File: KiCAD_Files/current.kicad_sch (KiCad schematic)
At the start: 10 parts, among them U3 ACS724xLCTR-10AB, U304 MCP6486UT-E/LT

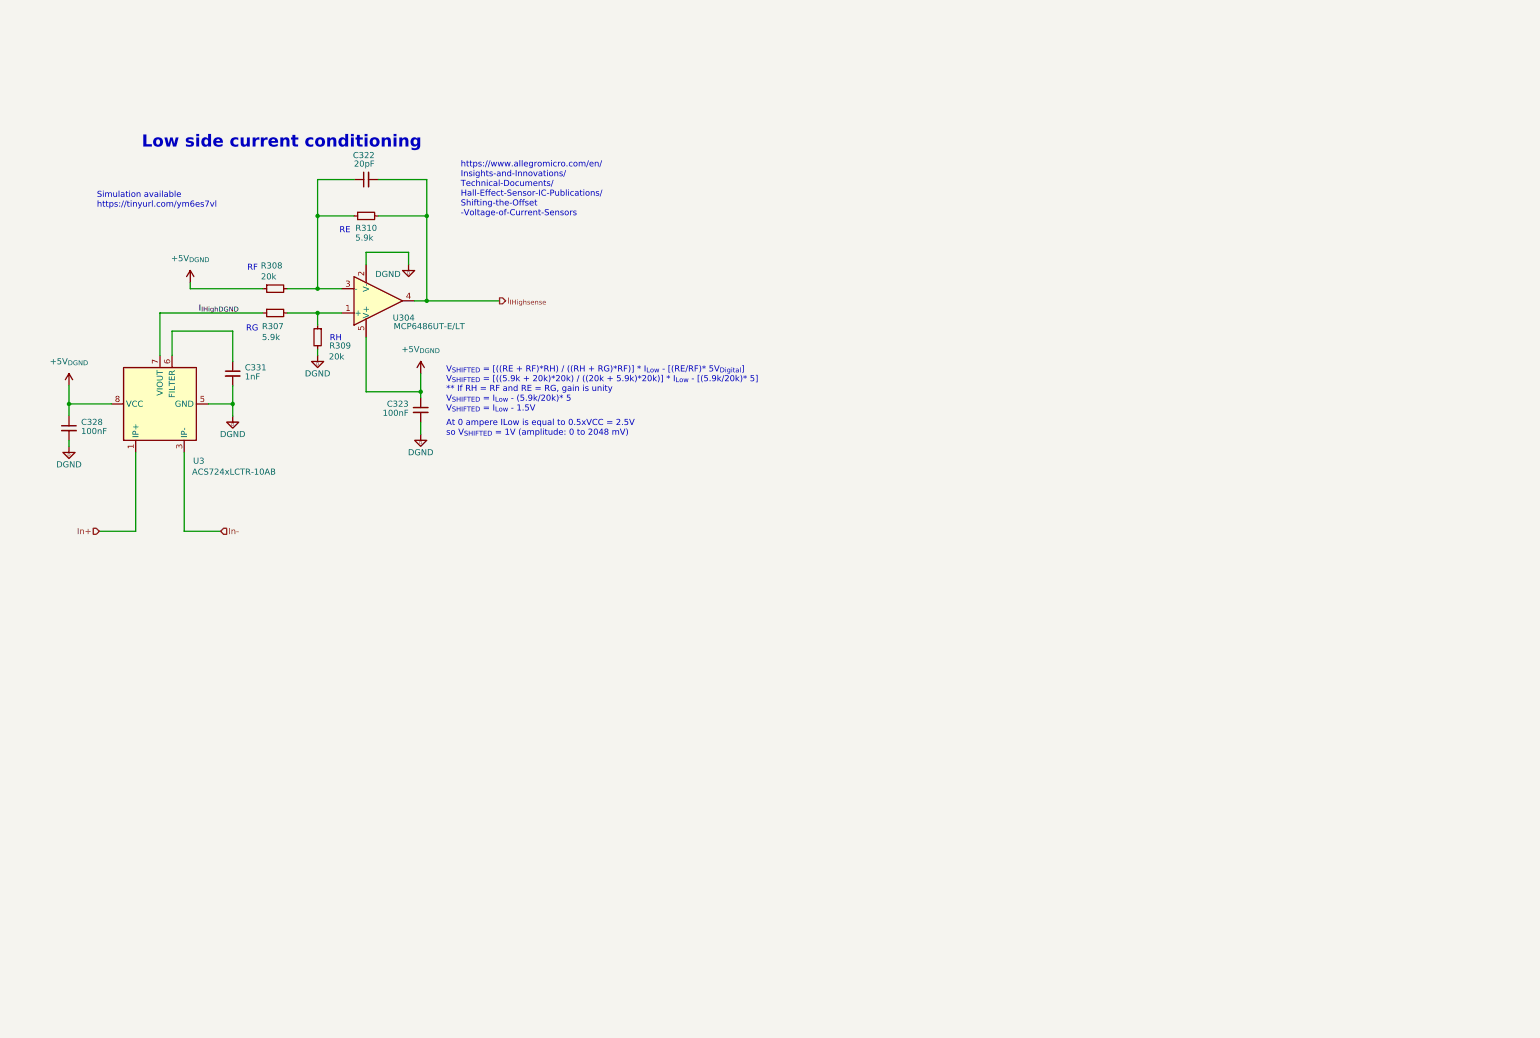
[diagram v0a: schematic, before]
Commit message: Schematic close to completion.
Signed-off-by: Jean Alinei <jean.alinei@owntech.org>
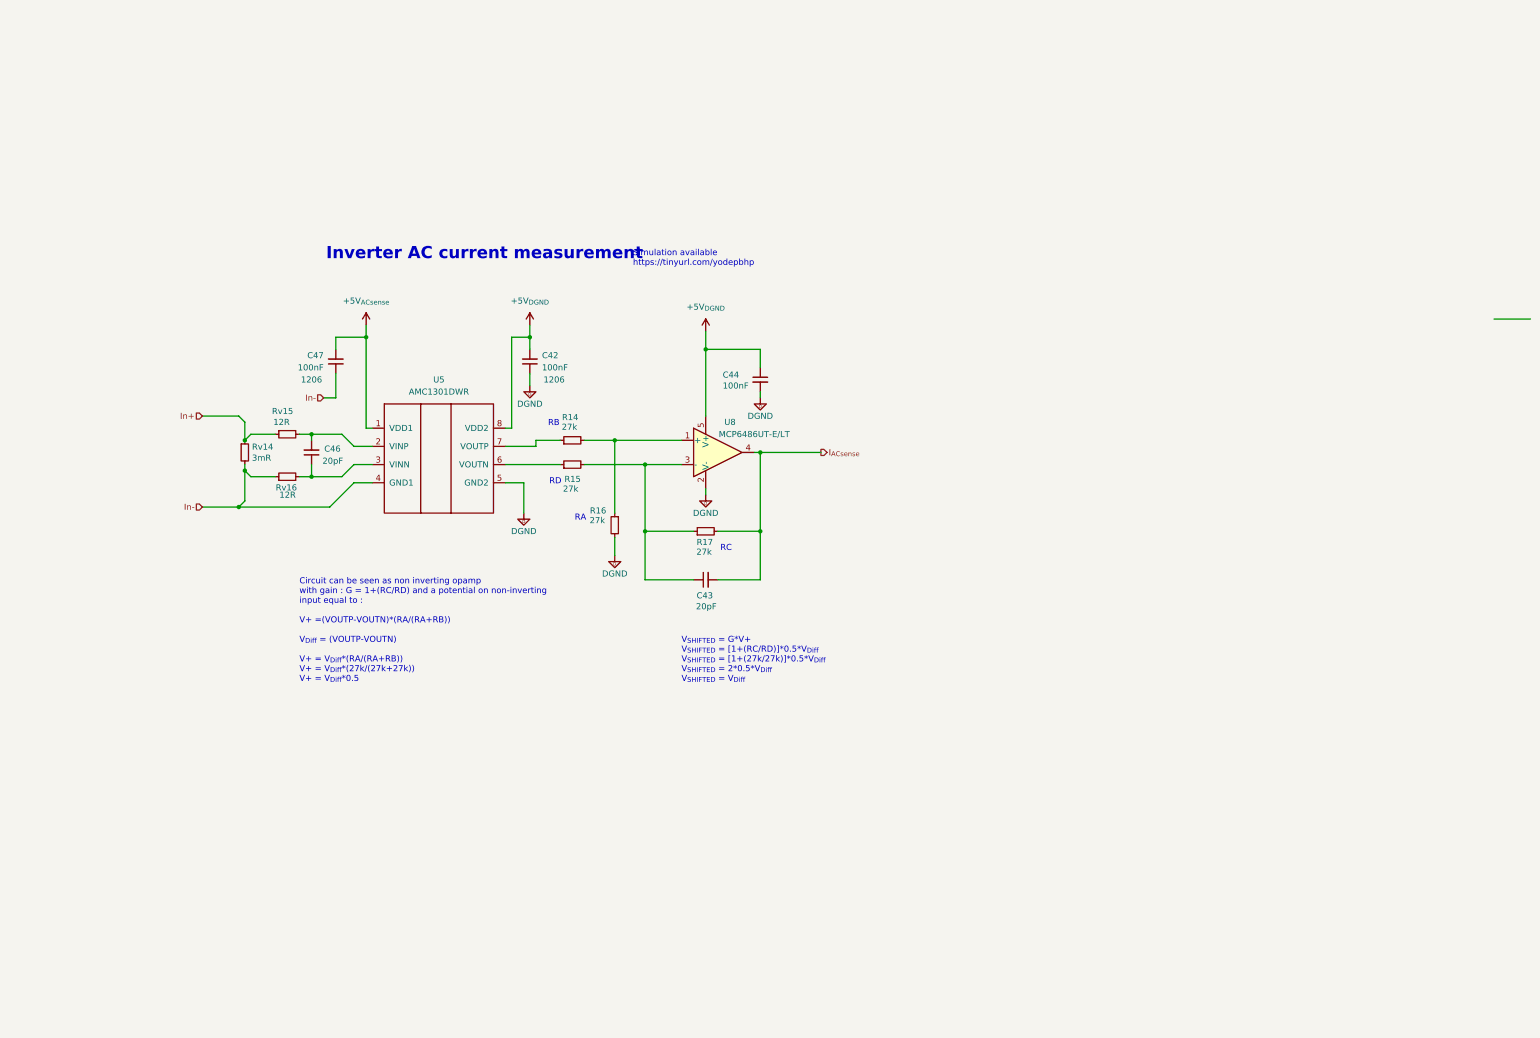
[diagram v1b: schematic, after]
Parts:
- removed C322: 20pF, Footprints:C_0805_2012Metric, symbol Device:C_Small
- removed C323, C328: 100nF, Capacitor_SMD:C_1206_3216Metric, symbol Device:C_Small
- removed C331: 1nF, Capacitor_SMD:C_1206_3216Metric, symbol Device:C_Small
- removed R307, R310: 5.9k, Footprints:R_0805_2012Metric, symbol Device:R_Small
- removed R308, R309: 20k, Footprints:R_0805_2012Metric, symbol Device:R_Small
- removed U3: ACS724xLCTR-10AB, Package_SO:SOIC-8_3.9x4.9mm_P1.27mm, symbol Sensor_Current:ACS724xLCTR-10AB
- removed U304: MCP6486UT-E/LT, Package_TO_SOT_SMD:SOT-353_SC-70-5_Handsoldering, symbol Symbols:MCP6486UT-E/LT
- added C42, C47: 100nF, Capacitor_SMD:C_1206_3216Metric, symbol Device:C_Small
- added C43, C46: 20pF, Footprints:C_0805_2012Metric, symbol Device:C_Small
- added C44: 100nF, Capacitor_SMD:C_0805_2012Metric, symbol Device:C_Small
- added R14, R15, R16, R17: 27k, Footprints:R_0805_2012Metric, symbol Device:R_Small
- added Rv14: 3mR, Resistor_SMD:R_0805_2012Metric, symbol Device:R_Small
- added Rv15, Rv16: 12R, Resistor_SMD:R_0805_2012Metric, symbol Device:R_Small
- added U5: AMC1301DWR, Package_SO:SOIC-8_7.5x5.85mm_P1.27mm, symbol Symbols:AMC1100
- added U8: MCP6486UT-E/LT, Package_TO_SOT_SMD:SOT-353_SC-70-5_Handsoldering, symbol Symbols:MCP6486UT-E/LT
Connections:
- net +5V_{DGND}: now also C42.2, C44.1, U5.8 (VDD2), U8.5 (V+)
- net DGND: now also C42.1, C44.2, R16.2, U5.5 (GND2), U8.2 (V-)
- net In+: now also Rv14.1, Rv15.1
- net In-: now also C47.1, Rv14.2, Rv16.1, U5.4 (GND1)
- new net: R14.1, U5.7 (VOUTP)
- new net: R14.2, R16.1, U8.1 (+)
- new net: C46.2, Rv15.2, U5.2 (VINP)
- new net: R15.1, U5.6 (VOUTN)
- new net: C43.1, R15.2, R17.1, U8.3 (-)
- new net: C46.1, Rv16.2, U5.3 (VINN)
- new net +5V_{ACsense}: C47.2, U5.1 (VDD1)
- new net I_{ACsense}: C43.2, R17.2, U8.4
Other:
- note added: "Circuit can be seen as non inverting opamp with gain : G = 1+(RC/RD) and a potential on non-inverting input equal to : V+ =(VOUTP-VOUTN)*(RA/(RA+RB)) V_{Diff} = (VOUTP-VOUTN) V+ = V_{Diff}*(RA/(RA+RB)) V+ = V_{Diff}*(27k/(27k+27k)) V+ = V_{Diff}*0.5"
- note added: "Inverter AC current measurement"
- note added: "RA"
- note added: "RB"
- note added: "RC"
- note added: "RD"
- note added: "Simulation available https://tinyurl.com/yodepbhp"
- note added: "V_{SHIFTED} = G*V+ V_{SHIFTED} = [1+(RC/RD)]*0.5*V_{Diff} V_{SHIFTED} = [1+(27k/27k)]*0.5*V_{Diff} V_{SHIFTED} = 2*0.5*V_{Diff} V_{SHIFTED} = V_{Diff}"
- note removed: "At 0 ampere ILow is equal to 0.5xVCC = 2.5V so V_{SHIFTED} = 1V (amplitude: 0 to 2048 mV)"
- note removed: "Low side current conditioning"
- note removed: "RE"
- note removed: "RF"
- note removed: "RG"
- note removed: "RH"
- note removed: "Simulation available https://tinyurl.com/ym6es7vl"
- note removed: "V_{SHIFTED} = [((RE + RF)*RH) / ((RH + RG)*RF)] * I_{Low} - [(RE/RF)* 5V_{Digital}] V_{SHIFTED} = [((5.9k + 20k)*20k) / ((20k + 5.9k)*20k)] * I_{Low} - [(5.9k/20k)* 5] ** If RH = RF and RE = RG, gain is unity V_{SHIFTED} = I_{Low} - (5.9k/20k)* 5 V_{SHIFTED} = I_{Low} - 1.5V"
- note removed: "https://www.allegromicro.com/en/ Insights-and-Innovations/ Technical-Documents/ Hall-Effect-Sensor-IC-Publications/ Shifting-the-Offset -Voltage-of-Current-Sensors"

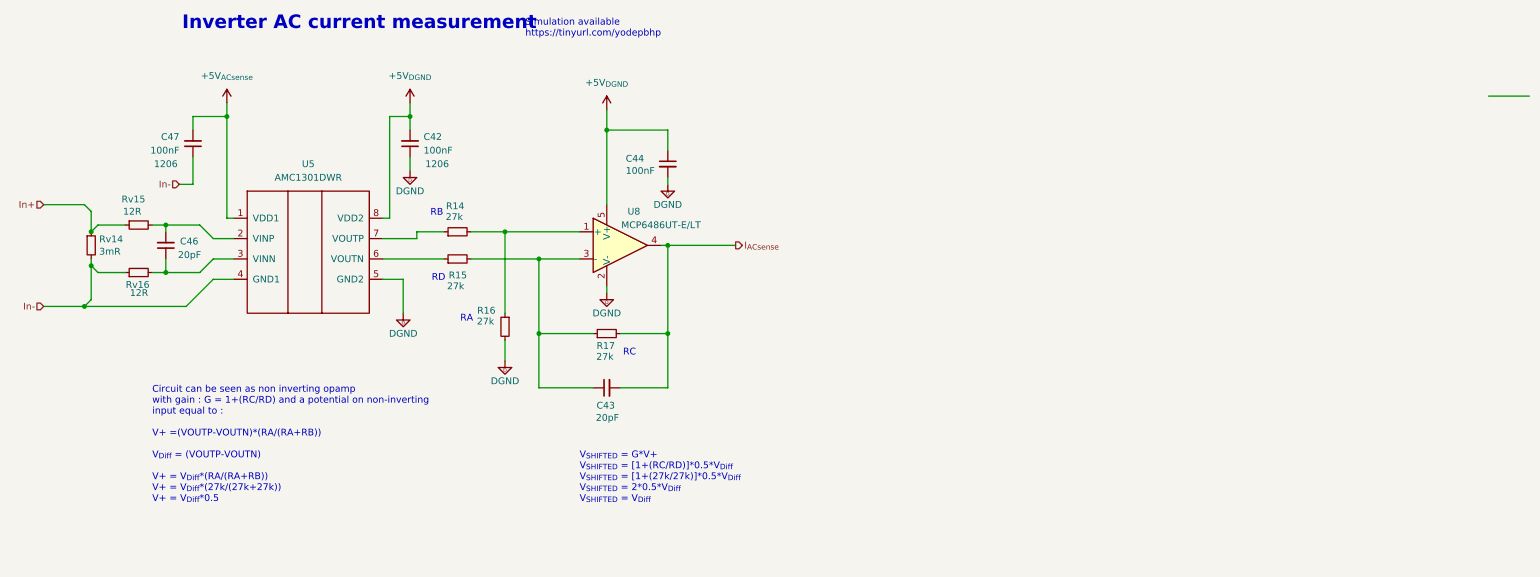
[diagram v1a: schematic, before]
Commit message: First routing pass complete.
Signed-off-by: Jean Alinei <jean.alinei@owntech.org>
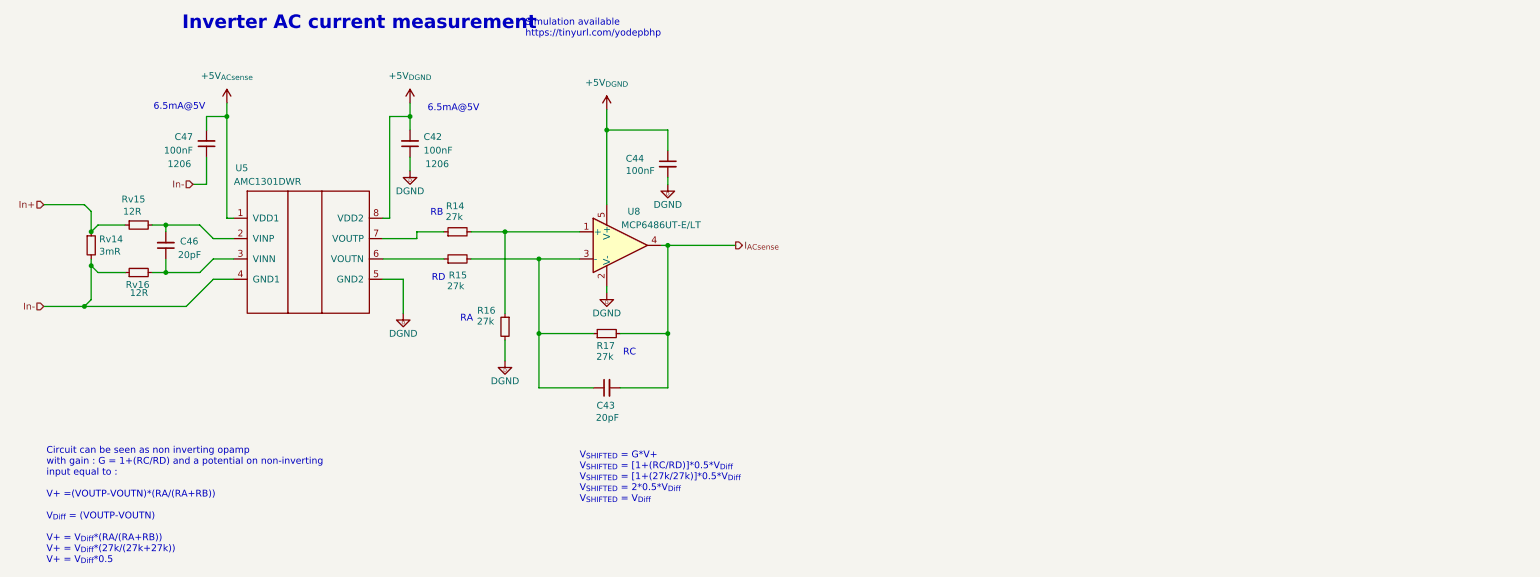
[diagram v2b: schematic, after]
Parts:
- Rv14: footprint Resistor_SMD:R_0805_2012Metric -> Resistor_SMD:R_2512_6332Metric
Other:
- note added: "6.5mA@5V"
- moved on the sheet: C47
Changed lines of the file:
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@@
+		)
+	)
+	(text "6.5mA@5V"
+		(exclude_from_sim no)
+		(at 132.588 84.836 0)
+		(effects
+			(font
+				(size 1.27 1.27)
+				(color 194 0 0 1)
+			)
 		)
 	)
@@
 	(text "Circuit can be seen as non inverting opamp\nwith gain : G = 1+(RC/RD) and a potential on non-inverting\ninput equal to :\n\nV+ =(VOUTP-VOUTN)*(RA/(RA+RB))\n\nV_{Diff} = (VOUTP-VOUTN)\n\nV+ = V_{Diff}*(RA/(RA+RB))\nV+ = V_{Diff}*(27k/(27k+27k))\nV+ = V_{Diff}*0.5"
 		(exclude_from_sim no)
-		(at 76.2 158.75 0)
+		(at 56.388 170.18 0)
 		(effects
 			(font
@@
 			)
 			(justify left bottom)
+		)
+	)
+	(text "6.5mA@5V"
+		(exclude_from_sim no)
+		(at 81.28 84.582 0)
+		(effects
+			(font
+				(size 1.27 1.27)
+				(color 194 0 0 1)
+			)
 		)
 	)
@@
 	(wire
 		(pts
-			(xy 83.82 86.36) (xy 90.17 86.36)
-		)
-		(stroke
-			(width 0)
-			(type default)
-		)
-	)
-	(wire
-		(pts
-			(xy 83.82 99.06) (xy 81.28 99.06)
+			(xy 86.36 86.36) (xy 90.17 86.36)
+		)
+		(stroke
+			(width 0)
+			(type default)
+		)
+	)
+	(wire
+		(pts
+			(xy 86.36 99.06) (xy 83.82 99.06)
 		)
 		(stroke
@@
 	(wire
 		(pts
-			(xy 83.82 93.98) (xy 83.82 99.06)
+			(xy 86.36 93.98) (xy 86.36 99.06)
 		)
 		(stroke
@@
 	(wire
 		(pts
-			(xy 83.82 86.36) (xy 83.82 88.9)
+			(xy 86.36 86.36) (xy 86.36 88.9)
 		)
 		(stroke
@@
 			(width 0)
 			(type default)
-		)
-	)
-	(wire
-		(pts
-			(xy 326.39 82.55) (xy 334.01 82.55)
-		)
-		(stroke
-			(width 0.5)
-			(type default)
-			(color 0 0 255 1)
 		)
 	)
 	(hierarchical_label "In-"
 		(shape input)
-		(at 81.28 99.06 180)
+		(at 83.82 99.06 180)
 		(effects
 			(font
@@
 		)
 	)
+	(rule_area
+		(polyline
+			(pts
+				(xy 105.41 73.66) (xy 105.41 146.05) (xy 200.66 146.05) (xy 200.66 73.66)
+			)
+			(stroke
+				(width 0)
+				(type dash)
+			)
+			(fill
+				(type none)
+			)
+		)
+	)
+	(netclass_flag ""
+		(length 2.54)
+		(shape round)
+		(at 115.57 146.05 0)
+		(fields_autoplaced yes)
+		(effects
+			(font
+				(size 1.27 1.27)
+			)
+			(justify left bottom)
+		)
+		(property "Netclass" "DGND"
+			(at 116.2685 143.51 0)
+			(effects
+				(font
+					(size 1.27 1.27)
+				)
+				(justify left)
+			)
+		)
+		(property "Component Class" ""
+			(at -143.51 97.79 0)
+			(effects
+				(font
+					(size 1.27 1.27)
+					(italic yes)
+				)
+				(hide yes)
+			)
+		)
+	)
 	(symbol
 		(lib_name "R_Small_14")
@@
 		(on_board yes)
 		(dnp no)
-		(fields_autoplaced yes)
 		(property "Reference" "U5"
-			(at 105.41 95.25 0)
+			(at 92.964 96.012 0)
 			(effects
 				(font
@@
 		)
 		(property "Value" "AMC1301DWR"
-			(at 105.41 97.79 0)
+			(at 97.79 98.552 0)
 			(effects
 				(font
@@
 			)
 		)
-		(property "Datasheet" "https://www.ti.com/lit/ds/symlink/amc1100.pdf?ts=1597048467257&ref_url=https%253A%252F%252Fwww.google.com%252F"
+		(property "Datasheet" "${KIPRJMOD}\\datasheets\\amc1301.pdf"
 			(at 105.41 119.38 0)
 			(effects
@@
 	(symbol
 		(lib_id "Device:C_Small")
-		(at 83.82 91.44 180)
+		(at 86.36 91.44 180)
 		(unit 1)
 		(exclude_from_sim no)
@@
 		(dnp no)
 		(property "Reference" "C47"
-			(at 81.28 90.17 0)
+			(at 83.82 90.17 0)
 			(effects
 				(font
@@
 		)
 		(property "Value" "100nF"
-			(at 81.28 92.71 0)
+			(at 83.82 92.71 0)
 			(effects
 				(font
@@
 		)
 		(property "Footprint" "Capacitor_SMD:C_1206_3216Metric"
-			(at 83.82 91.44 0)
+			(at 86.36 91.44 0)
 			(effects
 				(font
@@
 		)
 		(property "Datasheet" "${KIPRJMOD}\\datasheet\\KEM_C1002_X7R_SMD-3316098.pdf"
-			(at 83.82 91.44 0)
+			(at 86.36 91.44 0)
 			(effects
 				(font
@@
 		)
 		(property "Description" ""
-			(at 83.82 91.44 0)
+			(at 86.36 91.44 0)
 			(effects
 				(font
@@
 		)
 		(property "manf#" "C1206C104K5RAC7867"
-			(at 83.82 91.44 0)
+			(at 86.36 91.44 0)
 			(effects
 				(font
@@
 		)
 		(property "DNP" ""
-			(at 83.82 91.44 0)
+			(at 86.36 91.44 0)
 			(effects
 				(font
@@
 		)
 		(property "Voltage" "50V"
-			(at 85.09 87.63 90)
+			(at 87.63 87.63 90)
 			(effects
 				(font
@@
 		)
 		(property "Package" "1206"
-			(at 78.74 95.25 0)
+			(at 81.28 95.25 0)
 			(effects
 				(font
@@
 		)
 		(property "Functional Block" "Measurement"
-			(at 83.82 91.44 0)
+			(at 86.36 91.44 0)
 			(effects
 				(font
@@
 		)
 		(property "Metal content" "BaTiO3"
-			(at 83.82 91.44 0)
+			(at 86.36 91.44 0)
 			(effects
 				(font
@@
 		)
 		(property "Subfunction" "VIHigh measure"
-			(at 83.82 91.44 0)
+			(at 86.36 91.44 0)
 			(effects
 				(font
@@
 		)
 		(property "Dielectric" "X7R"
-			(at 83.82 91.44 0)
+			(at 86.36 91.44 0)
 			(effects
 				(font
@@
 		)
 		(property "Technology" ""
-			(at 83.82 91.44 0)
+			(at 86.36 91.44 0)
 			(effects
 				(font
@@
 		)
 		(property "LCSC" "C5449000"
-			(at 83.82 91.44 0)
+			(at 86.36 91.44 0)
 			(effects
 				(font
@@
 			)
 		)
-		(property "Footprint" "Resistor_SMD:R_0805_2012Metric"
+		(property "Footprint" "Resistor_SMD:R_2512_6332Metric"
 			(at 64.77 110.49 0)
 			(effects

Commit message: Added missing tracks for sensors and relay. Fixed many routing issues.
Signed-off-by: Jean Alinei <jean.alinei@owntech.org>
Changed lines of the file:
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@@
 	(wire
 		(pts
-			(xy 123.19 116.84) (xy 123.19 123.19)
+			(xy 124.46 116.84) (xy 124.46 132.08)
 		)
 		(stroke
@@
 	(wire
 		(pts
-			(xy 119.38 116.84) (xy 123.19 116.84)
+			(xy 119.38 116.84) (xy 124.46 116.84)
 		)
 		(stroke
@@
 	(symbol
 		(lib_id "Symbols:DGND")
-		(at 123.19 123.19 0)
+		(at 124.46 132.08 0)
 		(unit 1)
 		(exclude_from_sim no)
@@
 		(dnp no)
 		(property "Reference" "#PWR026"
-			(at 123.19 129.54 0)
+			(at 124.46 138.43 0)
 			(effects
 				(font
@@
 		)
 		(property "Value" "DGND"
-			(at 123.19 127 0)
+			(at 124.46 135.89 0)
 			(effects
 				(font
@@
 		)
 		(property "Footprint" ""
-			(at 123.19 123.19 0)
+			(at 124.46 132.08 0)
 			(effects
 				(font
@@
 		)
 		(property "Datasheet" ""
-			(at 123.19 123.19 0)
+			(at 124.46 132.08 0)
 			(effects
 				(font
@@
 		)
 		(property "Description" ""
-			(at 123.19 123.19 0)
-			(effects
-				(font
+			(at 124.46 132.08 0)
+			(effects
+				(font

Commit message: Added DRC rules according to IEC60664 and IPC2221.
Signed-off-by: Jean Alinei <jean.alinei@owntech.org>
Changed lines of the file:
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@@
 		(polyline
 			(pts
-				(xy 105.41 73.66) (xy 105.41 146.05) (xy 200.66 146.05) (xy 200.66 73.66)
+				(xy 102.87 146.05) (xy 102.87 73.66) (xy 25.4 73.66) (xy 25.4 146.05)
 			)
 			(stroke
@@
 		)
 	)
+	(rule_area
+		(polyline
+			(pts
+				(xy 106.68 73.66) (xy 106.68 146.05) (xy 201.93 146.05) (xy 201.93 73.66)
+			)
+			(stroke
+				(width 0)
+				(type dash)
+			)
+			(fill
+				(type none)
+			)
+		)
+	)
 	(netclass_flag ""
 		(length 2.54)
 		(shape round)
-		(at 115.57 146.05 0)
+		(at 116.84 146.05 0)
 		(fields_autoplaced yes)
 		(effects
@@
 		)
 		(property "Netclass" "DGND"
-			(at 116.2685 143.51 0)
+			(at 117.5385 143.51 0)
 			(effects
 				(font
@@
 		)
 		(property "Component Class" ""
-			(at -143.51 97.79 0)
+			(at -142.24 97.79 0)
+			(effects
+				(font
+					(size 1.27 1.27)
+					(italic yes)
+				)
+				(hide yes)
+			)
+		)
+	)
+	(netclass_flag ""
+		(length 2.54)
+		(shape round)
+		(at 92.71 146.05 0)
+		(fields_autoplaced yes)
+		(effects
+			(font
+				(size 1.27 1.27)
+			)
+			(justify left bottom)
+		)
+		(property "Netclass" "N"
+			(at 93.4085 143.51 0)
+			(effects
+				(font
+					(size 1.27 1.27)
+				)
+				(justify left)
+			)
+		)
+		(property "Component Class" ""
+			(at -166.37 97.79 0)
 			(effects
 				(font
@@
 		(dnp no)
 		(property "Reference" "U5"
-			(at 92.964 96.012 0)
+			(at 90.678 124.206 0)
 			(effects
 				(font
@@
 		)
 		(property "Value" "AMC1301DWR"
-			(at 97.79 98.552 0)
-			(effects
-				(font
+			(at 95.504 126.746 0)
+			(effects
+				(font
